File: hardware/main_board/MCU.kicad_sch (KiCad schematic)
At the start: 18 parts, among them J3 Conn_01x06_Pin, SW2 UP, U1 M0G3507QDGS32RQ1

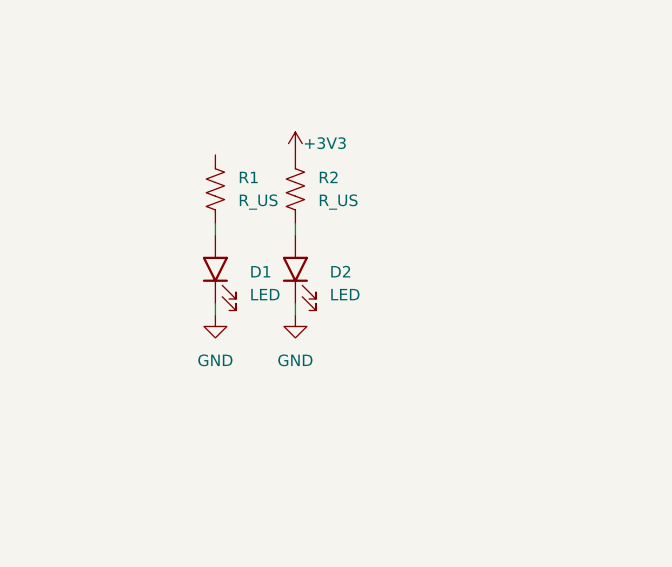
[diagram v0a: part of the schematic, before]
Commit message: fixed sides of peripheral board not being symmetrical. added teardrops. name of board tbd
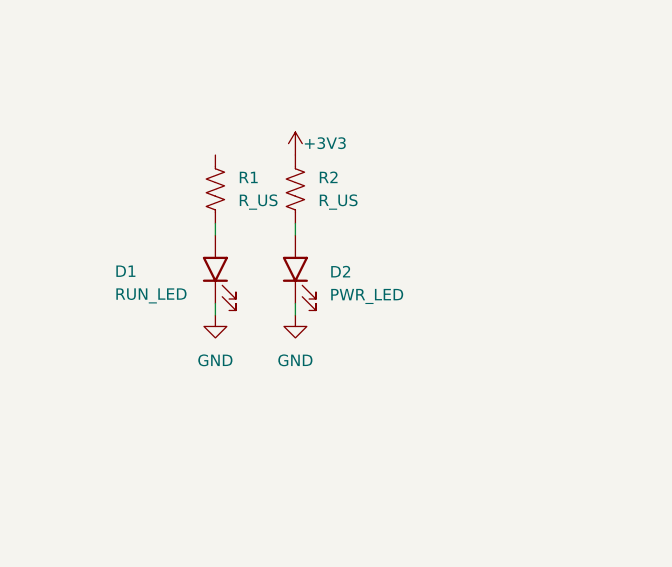
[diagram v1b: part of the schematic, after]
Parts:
- D1: value LED -> RUN_LED
- D2: value LED -> PWR_LED
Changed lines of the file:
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@@
 			)
 		)
-		(property "Value" "LED"
+		(property "Value" "PWR_LED"
 			(at 45.72 112.0774 0)
 			(effects
@@
 		(on_board yes)
 		(dnp no)
-		(fields_autoplaced yes)
 		(property "Reference" "D1"
-			(at 36.83 109.5374 0)
+			(at 21.844 109.474 0)
 			(effects
 				(font
@@
 			)
 		)
-		(property "Value" "LED"
-			(at 36.83 112.0774 0)
-			(effects
-				(font
+		(property "Value" "RUN_LED"
+			(at 21.844 112.014 0)
+			(effects
+				(font

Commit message: drew schematic
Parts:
- removed C12: 1uF, Capacitor_THT:C_Disc_D6.0mm_W2.5mm_P5.00mm, symbol Device:C
- removed R14, R16, R4: 0, Jumper:SolderJumper-2_P1.3mm_Open_RoundedPad1.0x1.5mm, symbol Device:R
- added C5: 1u, Capacitor_SMD:C_0805_2012Metric, symbol ECE445L:C
- added IC2: SN74HC157NSR, SOIC127P780X200-16N, symbol SamacSys_Parts:SN74HC157NSR
- added NT1: NetTie_2, symbol Device:NetTie_2
- C1: renamed from C9; footprint Capacitor_THT:C_Disc_D6.0mm_W2.5mm_P5.00mm -> Capacitor_SMD:C_0805_2012Metric
- C2: renamed from C4; footprint Capacitor_THT:C_Disc_D6.0mm_W2.5mm_P5.00mm -> Capacitor_SMD:C_0805_2012Metric
- C3: renamed from C7; footprint Capacitor_THT:C_Disc_D6.0mm_W2.5mm_P5.00mm -> Capacitor_SMD:C_0805_2012Metric
- C4: renamed from C8; footprint Capacitor_THT:C_Disc_D6.0mm_W2.5mm_P5.00mm -> Capacitor_SMD:C_0805_2012Metric
- D1, D2: footprint ECE445L:LED_D5.0mm -> 445L:LED_D5.0mm
- R1: renamed from R10; footprint Resistor_THT:R_Axial_DIN0204_L3.6mm_D1.6mm_P7.62mm_Horizontal -> Resistor_SMD:R_0805_2012Metric; symbol Device:R -> Device:R_US
- R2: renamed from R9; footprint Resistor_THT:R_Axial_DIN0204_L3.6mm_D1.6mm_P7.62mm_Horizontal -> Resistor_SMD:R_0805_2012Metric; symbol Device:R -> Device:R_US
- R3: renamed from R6; footprint Resistor_THT:R_Axial_DIN0204_L3.6mm_D1.6mm_P7.62mm_Horizontal -> Resistor_SMD:R_0805_2012Metric; symbol Device:R -> Device:R_US
- R4: renamed from R1; value R_US -> 470; footprint (none) -> Resistor_SMD:R_0805_2012Metric
- R5: renamed from R2; value R_US -> 470; footprint (none) -> Resistor_SMD:R_0805_2012Metric
- SW1: renamed from SW2; value UP -> RST; footprint ECE445L:SW_PUSH_6mm -> 445L:SW_PUSH_6mm
- renumbered U1 to IC1, J3 to J1
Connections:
- net PA10 is gone; now on net S0: IC1.17 (PA10/CLK_OUT)
- net PA11/SPI0_SCK is gone; now on net S1: IC1.18 (PA11)
- net PA12 is gone; now on net S2: IC1.19 (PA12/FCC_IN)
- net PA13/TFT_D/C is gone; now on net S3: IC1.20 (PA13)
- net PA14/SPI0_PICO is gone; now on net ADC_IN: IC1.21 (PA14/CLK_OUT/A0_12)
- net PA15/DACOUT is gone; now on net DAC_OUT: IC1.22 (PA15/A1_0/DACOUT)
- net PA16/SPI1_POCI is gone; now on net SPI1.MISO: IC1.23 (PA16/A1_1/FCC_IN)
- net PA17/SPI1_CLK is gone; now on net SPI1.SCK: IC1.24 (PA17/A1_2)
- net PA2 is gone; now on net CS_{P1}: IC1.9 (PA2/ROSC)
- net PA22 is gone; now on net CS_{P5}: IC1.29 (PA22/CLK_OUT/A0_7)
- net PA23 is gone; now on net CS_{P4}: IC1.30 (PA23/VREF+)
- net PA24/TFT_RESET is gone; now on net CS_{P3}: IC1.31 (PA24/A0_3)
- net PA25/SPI1_CS3 is gone; now on net CS_{SD}: IC1.32 (PA25/A0_2)
- net PA3 is gone; now on net CS_{P2}: IC1.10 (PA3/LFXIN)
- net PA4 is gone; now on net SPI0.MISO: IC1.11 (PA4/LFCLK_IN/LFXOUT)
- net PA5/HFXIN is gone; now on net SPI0.MOSI: IC1.12 (PA5/HFXIN/FCC_IN)
- net PA6/HFXOUT is gone; now on net SPI0.SCK: IC1.13 (PA6/HFCLK_IN/HFXOUT)
- net PA7 is gone; now on net LCD_DC: IC1.14 (PA7/CLK_OUT)
- net PA8/SPI0_CS0 is gone; now on net RUN_LED: IC1.15 (PA8)
- net PA9 is gone; now on net CS_{LCD}: IC1.16 (PA9/RTC_OUT/CLK_OUT)
- net GND: now also C5.2, IC2.15 (~{G}), IC2.8 (GND)
- net PA1: now also IC2.1 (~{A}/B)
- net SPI1.MOSI: now also NT1.2
- net RUN_LED: now reaches R4.1
- net PA18/SPI1_PICO/BSL_Invoke renamed BSL_INVOKE
- net BSL_INVOKE: now also NT1.1
- net PA21 renamed ENC_SW
- net ENC_SW: now also IC2.4 (1Y)
- net PA26 renamed ENC_CLK
- net ENC_CLK: now also IC2.9 (3Y)
- net PA27/SPI1_CS1 renamed ENC_DT
- net ENC_DT: now also IC2.7 (2Y)
- new net: C5.1, IC2.16 (VCC)
- new net ENC1.CLK: IC2.11 (3A)
- new net ENC1.DT: IC2.5 (2A)
- new net ENC1.SW: IC2.2 (1A)
- new net ENC2.CLK: IC2.10 (3B)
- new net ENC2.DT: IC2.6 (2B)
- new net ENC2.SW: IC2.3 (1B)
- no-connect marks 0 -> 3
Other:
- note added: "Encoder MUX"
- note added: "Hierarchical Labels"
- note added: "JTAG"
- note added: "LEDs"
- note added: "MCU"
- note added: "SPI0_CS0"
- note added: "SPI0_CS1"
- note added: "SPI0_CS2"
- note added: "lol"
- note added: "this is necessary bc we ran out of gpio lol idea is same as how our Hall ADC is set up except this will strobe between the two encoder inputs given a gpio clock"
- moved on the sheet: C1, C2, C3, C4, D1, D2, IC1, J1, R4, R5, SW1

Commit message: save before nuke SPI ADC
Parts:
- removed C5: 1u, Capacitor_SMD:C_0805_2012Metric, symbol ECE445L:C
- removed IC2: SN74HC157NSR, SOIC127P780X200-16N, symbol SamacSys_Parts:SN74HC157NSR
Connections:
- net CS_{LCD} renamed CS_LCD
- net CS_{P1} renamed CS_P0
- net CS_{P2} renamed CS_P1
- net CS_{P3} renamed CS_P2
- net CS_{P4} renamed CS_P3
- net CS_{P5} renamed CS_P4
- net CS_{SD} renamed CS_SD
- net ENC_CLK renamed ENC.CLK
- net ENC_DT renamed ENC.DT
- net ENC_SW renamed ENC.SW
- net PA1 renamed ENC_TOGGLE
- no-connect marks 3 -> 0
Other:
- note added: "TODO: ask rocco how debugger work with just chip"
- note removed: "Encoder MUX"
- note removed: "this is necessary bc we ran out of gpio lol idea is same as how our Hall ADC is set up except this will strobe between the two encoder inputs given a gpio clock"
- moved on the sheet: D1, D2, R4, R5

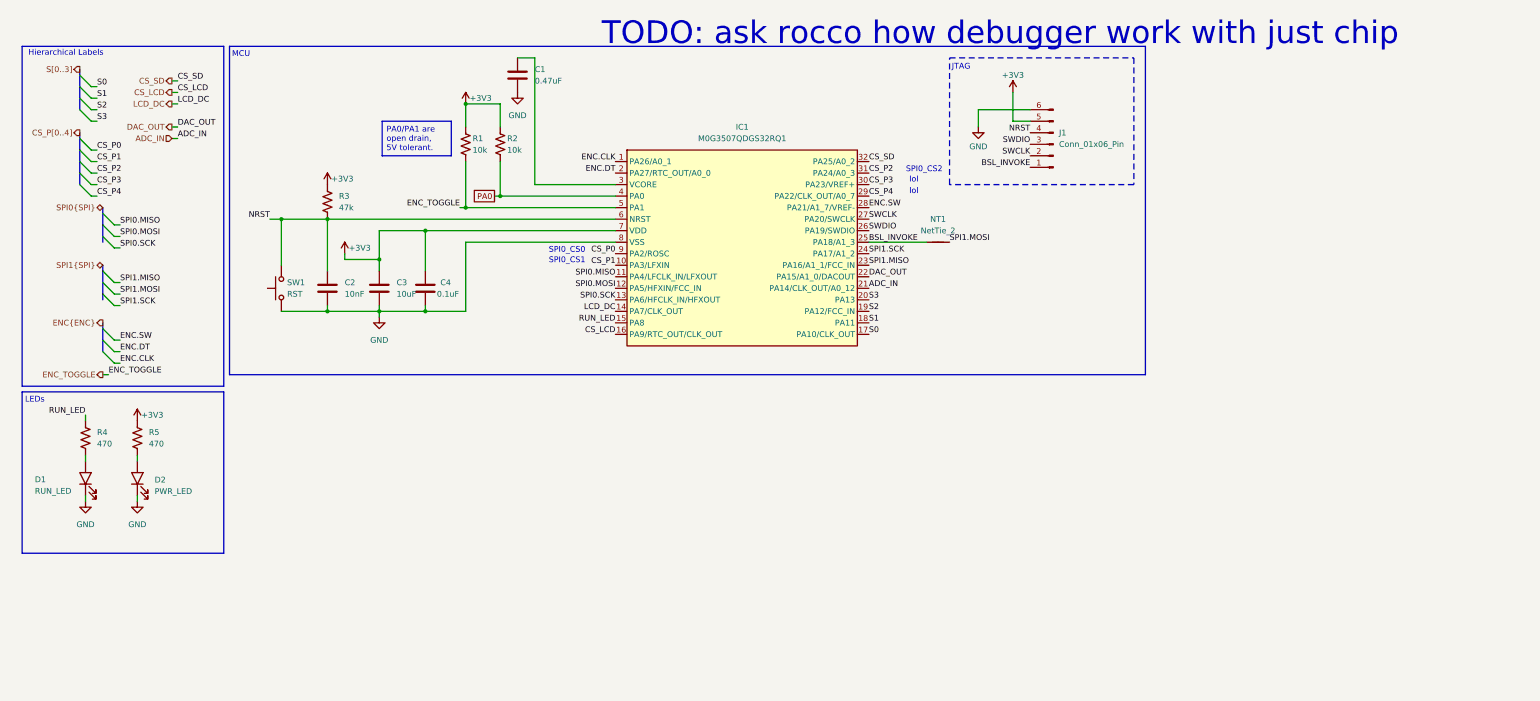
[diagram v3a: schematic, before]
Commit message: port to i2c for both boards. periph board passes drc
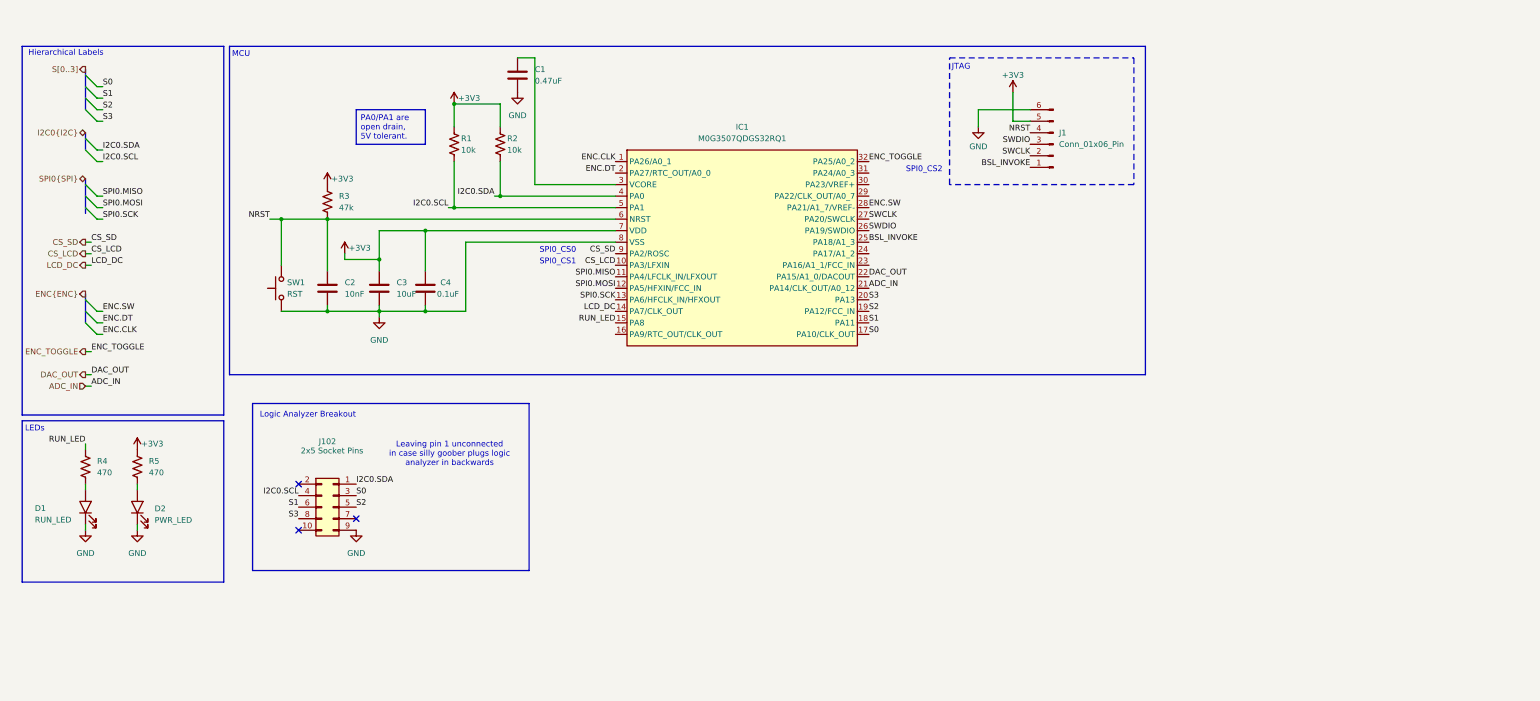
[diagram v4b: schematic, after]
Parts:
- removed NT1: NetTie_2, symbol Device:NetTie_2
- added J102: 2x5 Socket Pins, Connector_PinSocket_2.54mm:PinSocket_2x05_P2.54mm_Vertical, symbol SamacSys_Parts:Conn_02x05_Even_Odd
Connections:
- net CS_P0 is gone; now on net CS_SD: IC1.9 (PA2/ROSC)
- net CS_P1 is gone; now on net CS_LCD: IC1.10 (PA3/LFXIN)
- net CS_LCD: no longer IC1.16 (PA9/RTC_OUT/CLK_OUT)
- net CS_SD: no longer IC1.32 (PA25/A0_2)
- net ENC_TOGGLE: now also IC1.32 (PA25/A0_2); no longer IC1.5 (PA1), R1.1
- net GND: now also J102.9 (Pin_9)
- net S0: now also J102.3 (Pin_3)
- net S1: now also J102.6 (Pin_6)
- net S2: now also J102.5 (Pin_5)
- net S3: now also J102.8 (Pin_8)
- net CS_P2: no longer names the net of IC1.31 (PA24/A0_3)
- net CS_P3: no longer names the net of IC1.30 (PA23/VREF+)
- net CS_P4: no longer names the net of IC1.29 (PA22/CLK_OUT/A0_7)
- net PA0 renamed I2C0.SDA
- net I2C0.SDA: now also J102.1 (Pin_1)
- net SPI1.MISO: no longer names the net of IC1.23 (PA16/A1_1/FCC_IN)
- net SPI1.SCK: no longer names the net of IC1.24 (PA17/A1_2)
- new net I2C0.SCL: IC1.5 (PA1), J102.4 (Pin_4), R1.1
- no-connect marks 0 -> 3
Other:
- note added: "Leaving pin 1 unconnected in case silly goober plugs logic analyzer in backwards"
- note added: "Logic Analyzer Breakout"
- note removed: "TODO: ask rocco how debugger work with just chip"
- note removed: "lol"
- moved on the sheet: D1, D2, R1, R4, R5
